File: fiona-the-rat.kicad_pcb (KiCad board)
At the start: 2 copper layers, 79 parts, among them J1 XTAL_TP, J10 BMS_COUT_TP, J11 BMS_DOUT_TP, J12 BAT_P_JMP, J13 BAT_N_JMP, J14 GND_TP_2, J15 GND_TP_3, J16 USB_TP_N, J17 USB_TP_P, J2 USB_C_Receptacle_PowerOnly_6P, J3 GND_TP_1, J4 VBAT_ADC_TP, J5 ~{CHG}_TP, J6 +1V1_TP, J7 VBAT_TP, J8 +3V3_TP, J9 SWD, SW1 1825027-8, SW2 OS102011MA1QN1, U1 RP2040, U3 W25Q128JVSIQ, U4 BQ21040DBVR, U5 AP2112K-3.3, U6 CSD16406Q3, U7 CSD16406Q3, U8 BQ29700DSER, Y1 Crystal_GND24

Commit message: working on stuff
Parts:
- removed BT2: 1043P, 1043P:BAT_1043P
- added BT1: 1043P, 1043P:BAT_1043P, F.Cu at (170.2, 111.8)
- C25, C9, R10, R12, R13, TH1, U4, U5, U6, U7, U8: moved to B.Cu
- moved C26 146.2 mm to (124.5, 129.0), turned to -90 degrees
- moved C29 139.4 mm to (134.6, 139.2), turned to -90 degrees
- moved C19 137.1 mm to (133.6, 110.7), turned to -90 degrees
- moved C28 135.0 mm to (134.6, 129.0), turned to -90 degrees
- moved U7 132.5 mm to (171.2, 82.8), turned to -90 degrees
- moved C27 130.7 mm to (134.6, 118.6), turned to -90 degrees
- moved C20 130.5 mm to (139.7, 110.7), turned to 90 degrees
- moved C30 123.7 mm to (144.8, 129.0), turned to -90 degrees
- moved U6 123.6 mm to (171.2, 87.1), turned to 90 degrees
- moved U8 118.1 mm to (158.5, 84.8), turned to 90 degrees
- moved C16 116.0 mm to (133.6, 102.4), turned to 180 degrees
- moved U4 115.6 mm to (154.2, 84.8), turned to 180 degrees
- moved J13 112.7 mm to (170.2, 71.1), turned to 90 degrees
- moved SW_D1 106.5 mm to (139.7, 139.2)
- moved J11 103.3 mm to (162.3, 93.5)
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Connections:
- TH1 pad 2: Net-(J14-Pin_2) -> Net-(J13-Pin_2)
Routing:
- net Net-(J11-Pin_1): track 0.00 -> 88.1 mm
- net Net-(R12-Pad1): track 0.00 -> 78.8 mm
- net BACKLIGHT: track 0.00 -> 69.7 mm, vias 0 -> 1
- net LCD_RST: track 0.00 -> 65.2 mm, vias 0 -> 1
- net SD_CS: track 0.00 -> 59.1 mm
- net LCD_DCX: track 0.00 -> 57.4 mm
- net LCD_CS: track 0.00 -> 54.6 mm
- net LCD_MOSI: track 0.00 -> 53.9 mm
- net LCD_MISO: track 0.00 -> 52.8 mm, vias 0 -> 1
- net LCD_CLK: track 0.00 -> 48.3 mm, vias 0 -> 1
- net /UI_buttons/SW_D: track 0.00 -> 42.4 mm, vias 0 -> 3
- net /UI_buttons/SW_L: track 0.00 -> 38.2 mm
- net Net-(J13-Pin_2): track 0.00 -> 35.5 mm
- net /UI_buttons/SW_E: track 0.00 -> 34.9 mm
- net /UI_buttons/SW_R: track 0.00 -> 33.9 mm, vias 0 -> 1
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- added copper zone on B.Cu, net GND
- added copper zone on F.Cu, net GND
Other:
- board outline added: 83.3 x 89.9 mm

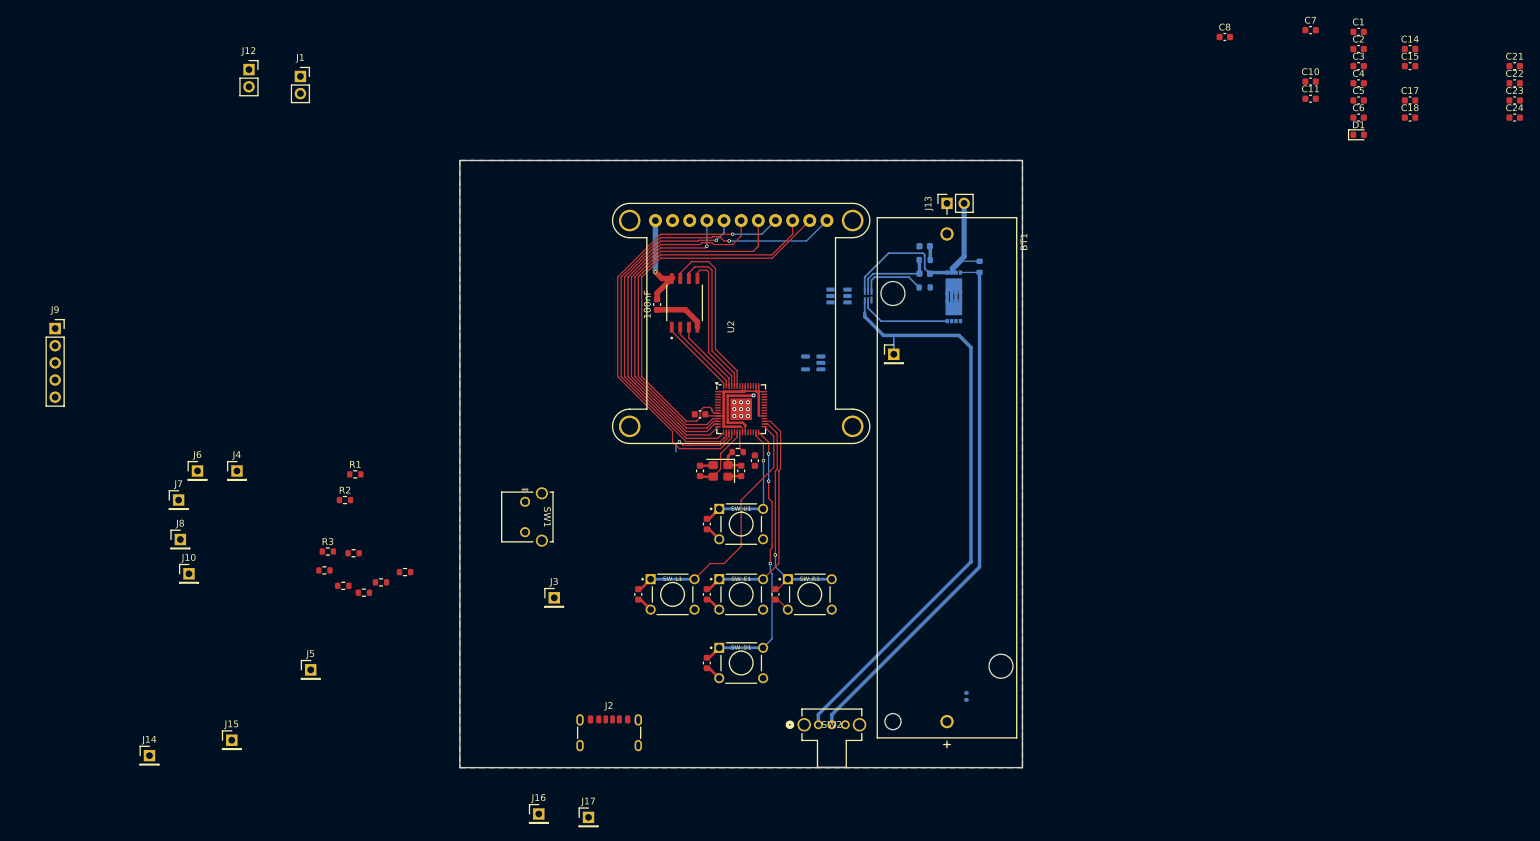
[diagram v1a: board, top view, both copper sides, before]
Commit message: placed all components
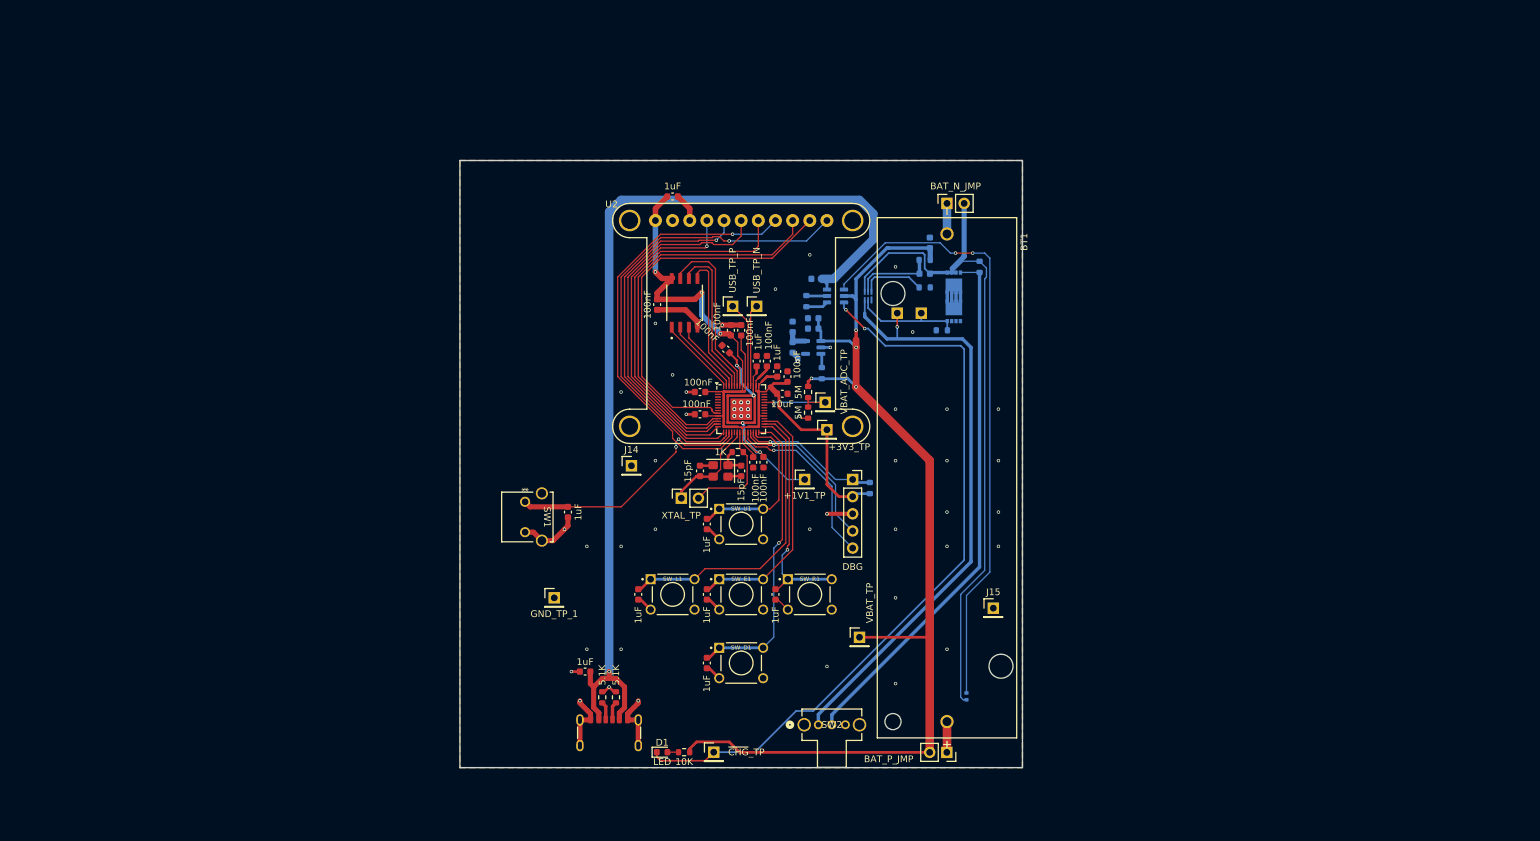
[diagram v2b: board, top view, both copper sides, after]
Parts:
- C10, C14, C15, C5, C7, J10, J11, R1, R11, R7, R8: moved to B.Cu
- J9: value SWD -> DBG
- moved C1 148.7 mm to (116.6, 140.5), turned to 180 degrees
- moved J12 144.6 mm to (170.2, 152.4), turned to -90 degrees
- moved D1 137.8 mm to (128.0, 152.4)
- moved C3 134.4 mm to (114.0, 116.8), turned to -90 degrees
- moved C23 128.1 mm to (133.6, 99.1), turned to 180 degrees
- moved J9 120.2 mm to (156.2, 112.0)
- moved C24 118.8 mm to (139.7, 89.9), turned to 90 degrees
- moved C22 118.1 mm to (143.5, 94.5), turned to 90 degrees
- moved C21 117.1 mm to (146.6, 96.8), turned to 90 degrees
- moved J10 115.1 mm to (166.4, 87.4)
- moved J15 114.5 mm to (177.0, 131.1)
- moved C18 105.4 mm to (138.2, 89.9), turned to 90 degrees
- moved C2 103.9 mm to (129.5, 70.1)
- moved J7 102.9 mm to (157.2, 135.4)
- moved C17 102.6 mm to (145.8, 99.3), turned to 180 degrees
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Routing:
- net VBAT: track 2.05 -> 156.4 mm, vias 0 -> 4
- net VBUS: track 0.00 -> 143.9 mm, vias 0 -> 1
- net ~{CHG}: track 0.00 -> 111.2 mm, vias 0 -> 2
- net /Battery management/TH: track 0.00 -> 91.7 mm, vias 0 -> 2
- net +3V3: track 41.2 -> 128.1 mm, vias 1 -> 3
- net Net-(J13-Pin_2): track 35.5 -> 103.1 mm
- net GND: track 35.9 -> 87.3 mm, vias 9 -> 50
- net +1V1: track 11.7 -> 50.6 mm, vias 1 -> 4
- net SWCLK: track 0.00 -> 26.8 mm, vias 0 -> 1
- net Net-(U1-GPIO14): track 10.4 -> 37.1 mm, vias 1 -> 2
- net SWD: track 0.00 -> 24.1 mm, vias 0 -> 1
- net ~{RESET}: track 0.00 -> 20.7 mm, vias 0 -> 1
- net Net-(J4-Pin_1): track 0.00 -> 13.2 mm, vias 0 -> 1
- net XTAL_OUT: track 3.13 -> 16.2 mm
- net /USB_DP: track 0.00 -> 12.7 mm
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
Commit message: adding stuff
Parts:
- added C31: 1uF, Capacitor_SMD:C_0603_1608Metric, F.Cu at (114.3, 112.0)
- added C32: 1uF, Capacitor_SMD:C_0603_1608Metric, F.Cu at (114.3, 101.9)
- added C33: 1uF, Capacitor_SMD:C_0603_1608Metric, F.Cu at (114.3, 91.7)
- added C34: 1uF, Capacitor_SMD:C_0603_1608Metric, F.Cu at (114.3, 81.5)
- added C35: 1uF, Capacitor_SMD:C_0603_1608Metric, F.Cu at (114.3, 71.4)
- added J6: Periph, Connector_JST:JST_XH_B2B-XH-A_1x02_P2.50mm_Vertical, F.Cu at (106.7, 146.1)
- added MOSFET1: DMN3042L-7, DMN3042L-7-footprints:SOT23_DMN3042L_DIO, F.Cu at (106.7, 139.7)
- added R6: 10K, Resistor_SMD:R_0603_1608Metric, F.Cu at (110.2, 139.7)
- added REF**: MountingHole_2.2mm_M2, MountingHole:MountingHole_2.2mm_M2, F.Cu at (178.6, 67.6)
- added REF**: MountingHole_2.2mm_M2, MountingHole:MountingHole_2.2mm_M2, F.Cu at (100.8, 151.9)
- added REF**: MountingHole_2.2mm_M2, MountingHole:MountingHole_2.2mm_M2, F.Cu at (178.6, 151.9)
- added REF**: MountingHole_2.2mm_M2, MountingHole:MountingHole_2.2mm_M2, F.Cu at (100.8, 67.6)
- added WLED1: WS2812B, LED_SMD:LED_WS2812B_PLCC4_5.0x5.0mm_P3.2mm, F.Cu at (114.3, 108.5)
- added WLED2: WS2812B, LED_SMD:LED_WS2812B_PLCC4_5.0x5.0mm_P3.2mm, F.Cu at (114.3, 98.3)
- added WLED3: WS2812B, LED_SMD:LED_WS2812B_PLCC4_5.0x5.0mm_P3.2mm, F.Cu at (114.3, 88.1)
- added WLED4: WS2812B, LED_SMD:LED_WS2812B_PLCC4_5.0x5.0mm_P3.2mm, F.Cu at (114.3, 78.0)
- added WLED5: WS2812B, LED_SMD:LED_WS2812B_PLCC4_5.0x5.0mm_P3.2mm, F.Cu at (114.3, 67.8)
- J14: renamed from J9; value DBG -> SWD
- TH1: moved to F.Cu
- moved J10 1.98 mm to (134.1, 151.1)
- moved D1 1.78 mm to (128.0, 150.6)
- moved R7 1.28 mm to (131.1, 151.1), turned to -90 degrees
- moved TH1 0.15 mm to (173.0, 144.0)
- renumbered J17 to J1, J5 to J10, J6 to J11, J7 to J12, J8 to J13, J10 to J15, J11 to J16, J12 to J17, J13 to J18, J16 to J2, J1 to J3, J2 to J4, J4 to J5, J3 to J7, J14 to J8, J15 to J9, R9 to R10, R10 to R11, R11 to R12, R12 to R13, R13 to R14, R6 to R7, R7 to R8, R8 to R9
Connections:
- U1 pad 5: unconnected-(U1-GPIO3-Pad5) -> /LEDs/DIN
- U1 pad 6: unconnected-(U1-GPIO4-Pad6) -> Net-(MOSFET1-G)
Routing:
- net VBAT: track 156.4 -> 290.6 mm, vias 4 -> 5
- net Net-(MOSFET1-G): track 0.00 -> 55.4 mm, vias 0 -> 2
- net /LEDs/DIN: track 0.00 -> 23.8 mm, vias 0 -> 2
- net +3V3: track 128.1 -> 147.0 mm, vias 3 -> 4
- net Net-(WLED1-DOUT): track 0.00 -> 15.5 mm
- net Net-(WLED2-DOUT): track 0.00 -> 15.5 mm
- net Net-(WLED4-DOUT): track 0.00 -> 15.5 mm
- net Net-(WLED3-DOUT): track 0.00 -> 15.5 mm
- net GND: track 87.3 -> 96.2 mm, vias 50 -> 70
- net Net-(J6-Pin_1): track 0.00 -> 6.72 mm
- net Net-(J18-Pin_2): track 103.1 -> 104.6 mm, vias 0 -> 1
- net Net-(D1-A): track 1.65 -> 2.39 mm
- net /Battery management/TH: vias 2 -> 3
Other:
- board text added: "+1V1_TP"
- board text added: "+3V3_TP"
- board text added: "3V3"
- board text added: "BAT_N_JMP"
- board text added: "BAT_P_JMP"
- board text added: "GND"
- board text added: "GND_TP_1"
- board text added: "GND_TP_2"
- board text added: "SWC"
- board text added: "SWD"
- board text added: "USB_TP_N"
- board text added: "USB_TP_P"
- board text added: "VBAT_ADC_TP"
- board text added: "VBAT_TP"
- board text added: "~{CHG}_TP"
- board text added: "~{RST}"

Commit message: tweaking
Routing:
- net GND: track 96.2 -> 122.4 mm, vias 70 -> 98
